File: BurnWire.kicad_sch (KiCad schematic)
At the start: 26 parts, among them J1 Conn_01x06_Pin, J2 282834-2, J3 Conn_01x02_Pin, J4 Conn_01x01_Pin, U1 ADP2303ARDZ

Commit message: Fix unrouted areas, board dimensions
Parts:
- C3, C4, C5: footprint Capacitor_SMD:C_0805_2012Metric_Pad1.18x1.45mm_HandSolder -> Capacitor_SMD:CP_Elec_5x5.4

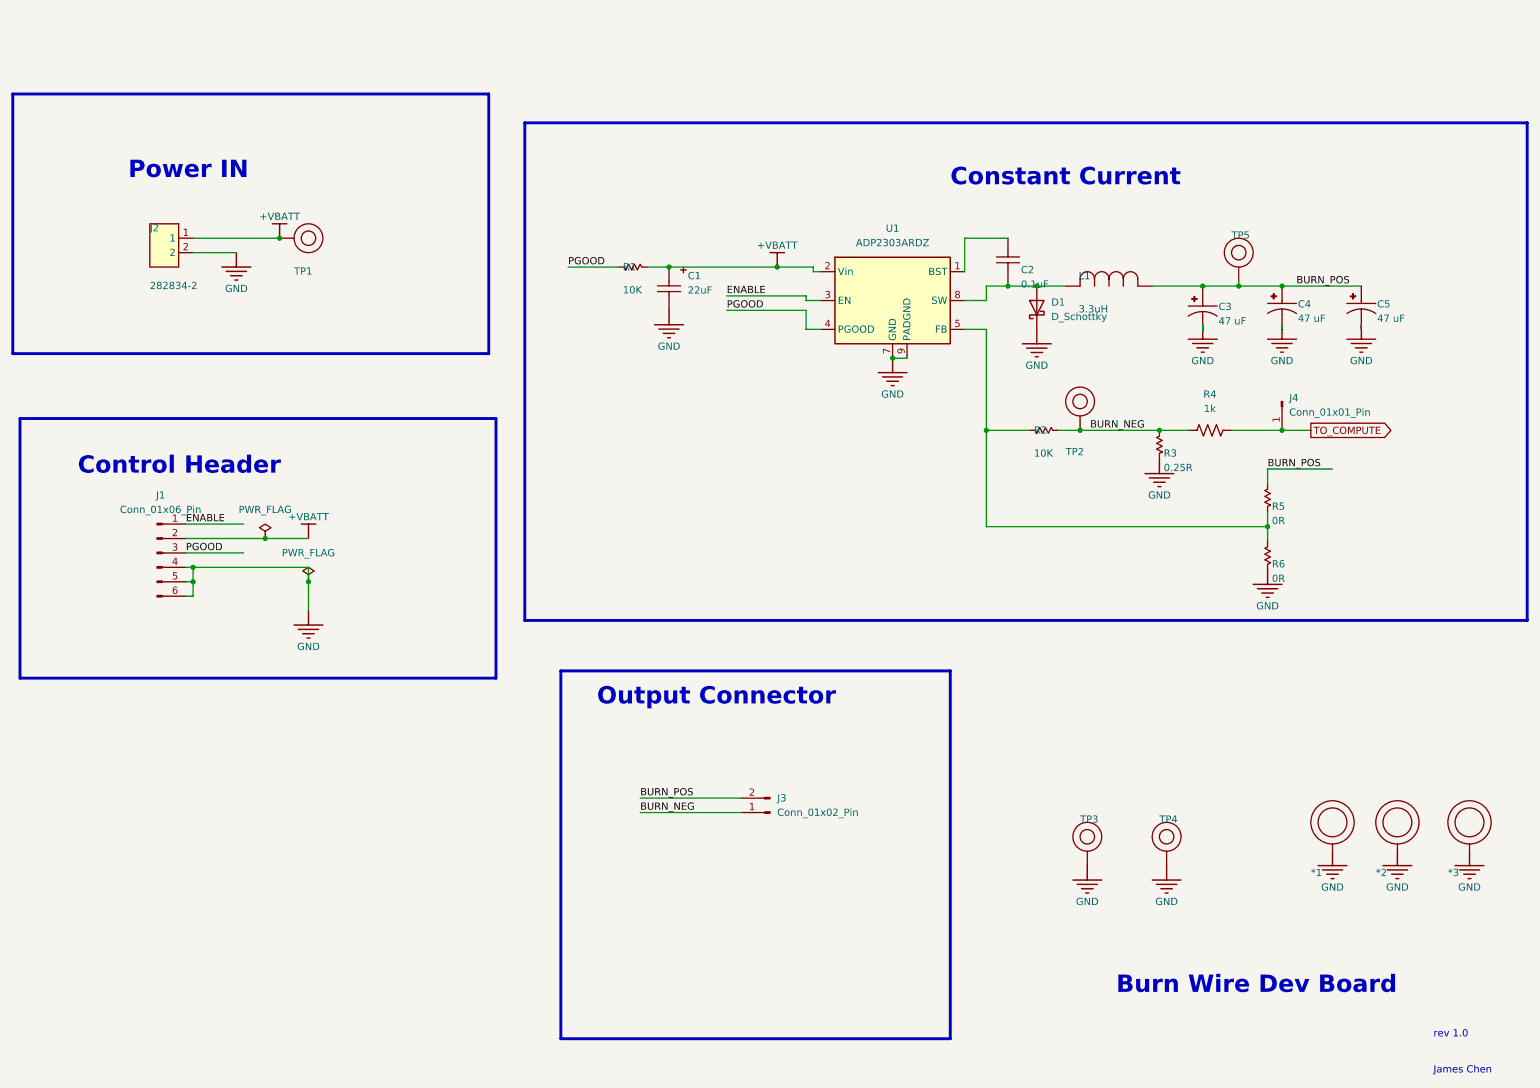
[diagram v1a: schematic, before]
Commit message: Removed all Altium references, fixed D1 direction, prepare for Rev 4.0
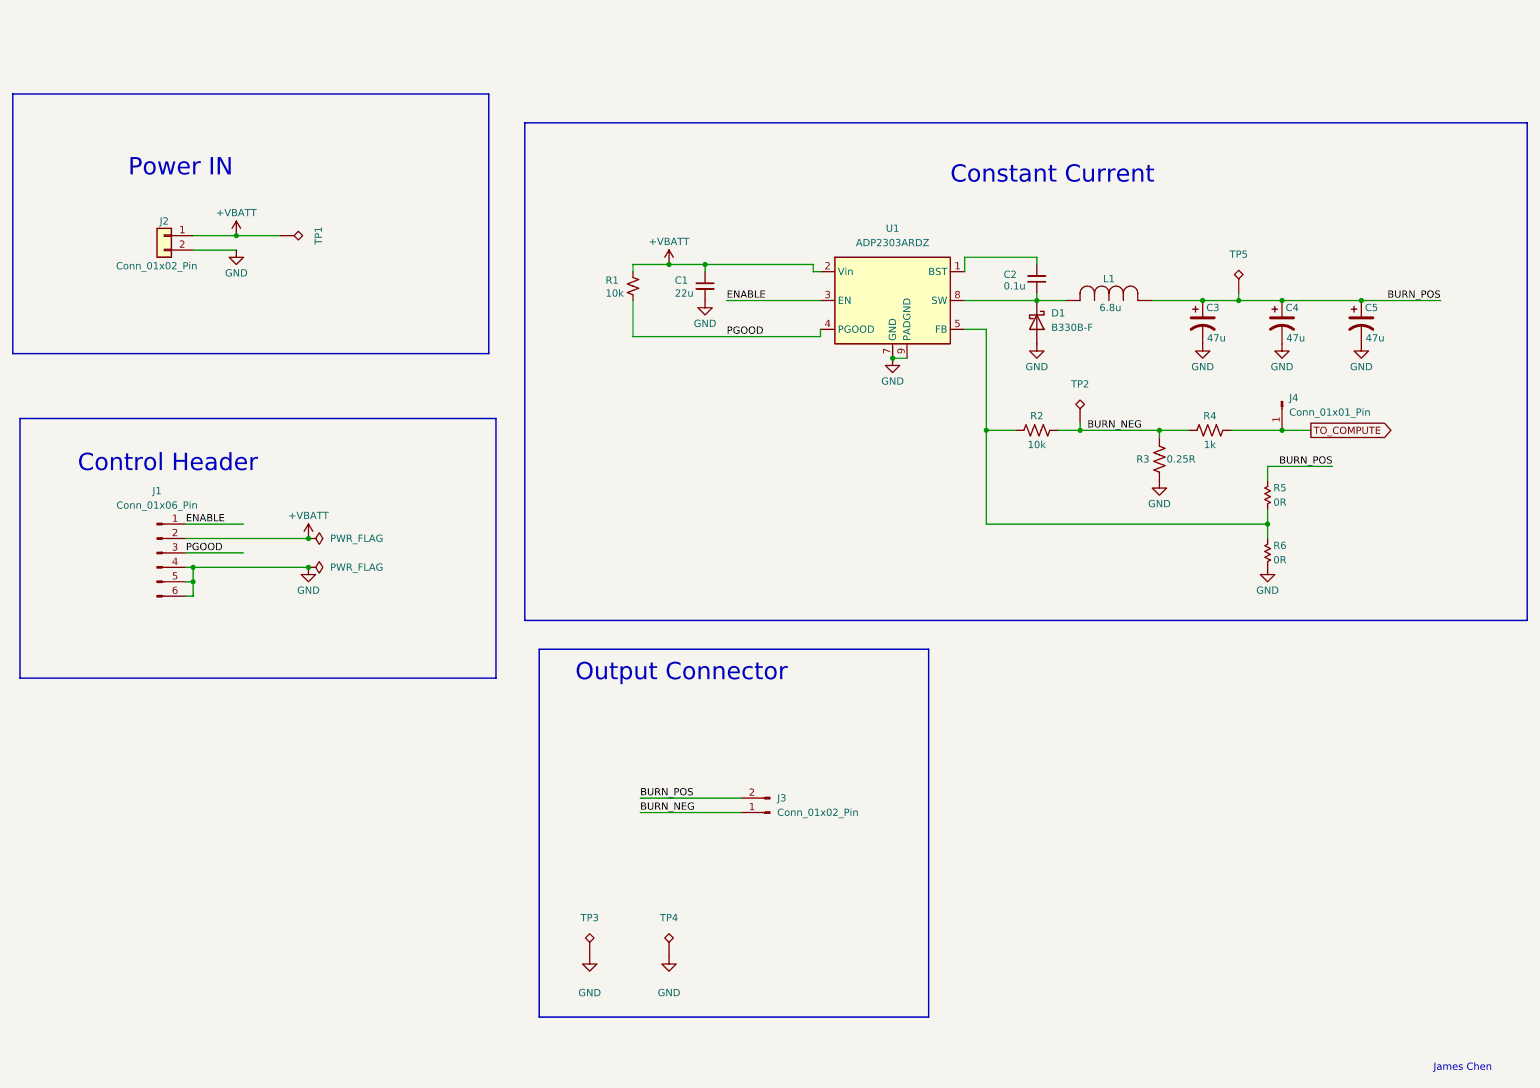
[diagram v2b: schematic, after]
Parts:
- removed *1, *2, *3: M2 Mounting, symbol RCU Board rev1.0:root_1_M2 Mounting_RCU Board rev1.0.SchLib
- C1: value 22uF -> 22u; symbol Burn Wire Dev Board:root_3_CT-225-M-20V-OTH-1206_Burn Wire Dev Board.SchLib -> Device:C_Small; ALTIUM_VALUE 22uF -> (none); COMPONENTLINK1DESCRIPTION Datasheet -> (none); COMPONENTLINK1URL * -> (none); COMPONENTLINK2DESCRIPTION Manufacturer Website -> (none); COMPONENTLINK2URL * -> (none); PART DESCRIPTION CAP TANT 22UF 10% 10V 1206 -> (none)
- C2: value 0.1uF -> 0.1u; symbol Burn Wire Dev Board:root_1_CC-104-K-25V-X7R-0603_Burn Wire Dev Board.SchLib -> Device:C_Small; ALTIUM_VALUE 0.1uF -> (none); COMPONENTLINK1DESCRIPTION Datasheet -> (none); COMPONENTLINK1URL https://ds.yuden.co.jp/TYCOMPAS/ut/detail?pn=TMK105BJ104KV-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 -> (none); COMPONENTLINK2DESCRIPTION Manufacturer Website -> (none); COMPONENTLINK2URL https://www.yuden.co.jp/or/ -> (none); PART DESCRIPTION 0.1 µF ±10% 25V Ceramic Capacitor X7R 0603 (1608 Metric) -> (none)
- C3, C4, C5: value 47 uF -> 47u; symbol Burn Wire Dev Board:root_3_CC-25SVPF47M_Burn Wire Dev Board.SchLib -> Device:C_Polarized_US; ALTIUM_VALUE 47 uF -> (none); COMPONENTLINK1DESCRIPTION Datasheet -> (none); COMPONENTLINK1URL * -> (none); COMPONENTLINK2DESCRIPTION Manufacture Website -> (none); COMPONENTLINK2URL * -> (none); PART DESCRIPTION CAP ALUM POLY 47UF 20% 25V SMD -> (none)
- D1: value D_Schottky -> B330B-F; footprint burn_wire:CR_SMB_320-345BE_DIO-L -> footprints:CR_SMB_320-345BE_DIO-L; DISTRIBUTOR (none) -> Digikey; DISTRIBUTOR PART # (none) -> B330B-FDICT-ND; MANUFACTURER (none) -> Diodes Incorporated; MANUFACTURER PART # (none) -> B330B-13-F
- J2: value 282834-2 -> Conn_01x02_Pin; symbol Burn Wire Dev Board:root_0_mirrored_J-282834-2_Burn Wire Dev Board.SchLib -> Connector_Generic:Conn_01x02
- L1: value 6.8 UH -> 6.8u; footprint burn_wire:IND_BOURNS_SRN6045 -> footprints:IND_BOURNS_SRN6045; symbol Burn Wire Dev Board:root_0_L-IHLP4040DZER6R8M01_Burn Wire Dev Board.SchLib -> imported_symbols:L-IHLP4040DZER6R8M01; ALTIUM_VALUE 3.3uH -> (none)
- R1: value 10K -> 10k; symbol Burn Wire Dev Board:root_0_RT-10K0-F-1/16W-0603_Burn Wire Dev Board.SchLib -> Device:R_Small_US; ALTIUM_VALUE 10K -> (none); COMPONENTLINK1DESCRIPTION Datasheet -> (none); COMPONENTLINK1URL https://www.vishay.com/docs/20035/dcrcwe3.pdf -> (none); COMPONENTLINK2DESCRIPTION Manufacturer Website -> (none); COMPONENTLINK2URL https://www.vishay.com/ -> (none); PART DESCRIPTION RES 10K OHM 1% 1/8W 0603 -> (none)
- R2: value 10K -> 10k; symbol Burn Wire Dev Board:root_0_RT-10K0-F-1/16W-0603_Burn Wire Dev Board.SchLib -> Device:R_US; ALTIUM_VALUE 10K -> (none); COMPONENTLINK1DESCRIPTION Datasheet -> (none); COMPONENTLINK1URL https://www.vishay.com/docs/20035/dcrcwe3.pdf -> (none); COMPONENTLINK2DESCRIPTION Manufacturer Website -> (none); COMPONENTLINK2URL https://www.vishay.com/ -> (none); PART DESCRIPTION RES 10K OHM 1% 1/8W 0603 -> (none)
- R3: symbol Burn Wire Dev Board:root_1_RT-0.25R0-F-3W-2010_Burn Wire Dev Board.SchLib -> Device:R_US; ALTIUM_VALUE 0.25R -> (none); COMPONENTLINK1DESCRIPTION Datasheet -> (none); COMPONENTLINK1URL https://www.vishay.com/docs/20035/dcrcwe3.pdf -> (none); COMPONENTLINK2DESCRIPTION Manufacturer Website -> (none); COMPONENTLINK2URL https://www.vishay.com/ -> (none); DISTRIBUTOR PART # 541-10112-1-ND -> 541-WSLT2010R2500FEA18CT-ND; MANUFACTURER PART # WSLT2010R5000FEA18 -> WSLT2010R2500FEA18; PART DESCRIPTION RES 0.5 OHM 1% 1W 2010 -> (none)
- R5, R6: symbol Burn Wire Dev Board:root_1_RT-0R00-F-1/10W-0603_Burn Wire Dev Board.SchLib -> imported_symbols:R_Small_US_Alt; ALTIUM_VALUE 0R -> (none); COMPONENTLINK1DESCRIPTION Datasheet -> (none); COMPONENTLINK1URL https://industrial.panasonic.com/ww/products/resistors/chip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 -> (none); COMPONENTLINK2DESCRIPTION Manufacturer Website -> (none); COMPONENTLINK2URL https://industrial.panasonic.com/ww/products/resistors/chip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 -> (none); PART DESCRIPTION 0 Ohms Jumper 0.1W, 1/10W Chip Resistor 0603 (1608 Metric) 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 -> (none)
- TP1: footprint Connector_PinSocket_2.54mm:PinSocket_1x01_P2.54mm_Vertical -> TestPoint:TestPoint_Loop_D1.80mm_Drill1.0mm_Beaded; symbol PowerManagmentBoard_V4.0:root_0_TP_PowerManagmentBoard_V4.0.SchLib -> Connector:TestPoint_Alt; COMPONENTLINK1DESCRIPTION Datasheet -> (none); COMPONENTLINK1URL https://industrial.panasonic.com/ww/products/resistors/chip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 -> (none); COMPONENTLINK2DESCRIPTION Manufacturer Website -> (none); COMPONENTLINK2URL https://industrial.panasonic.com/ww/products/resistors/chip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 -> (none)
- TP2, TP3, TP4, TP5: footprint Connector_PinSocket_2.54mm:PinSocket_1x01_P2.54mm_Vertical -> TestPoint:TestPoint_Loop_D1.80mm_Drill1.0mm_Beaded; symbol PowerManagmentBoard_V4.0:root_1_TP_PowerManagmentBoard_V4.0.SchLib -> Connector:TestPoint_Alt; COMPONENTLINK1DESCRIPTION Datasheet -> (none); COMPONENTLINK1URL https://industrial.panasonic.com/ww/products/resistors/chip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 -> (none); COMPONENTLINK2DESCRIPTION Manufacturer Website -> (none); COMPONENTLINK2URL https://industrial.panasonic.com/ww/products/resistors/chip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 -> (none)
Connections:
- net GND: now also D1.2 (A); no longer D1.1 (K)
- net at C2.1, L1.2, U1.8 (SW): now also D1.1 (K); no longer D1.2 (A)
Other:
- note removed: "Burn Wire Dev Board"
- note removed: "rev 1.0"
- moved on the sheet: D1, J2, L1, R1, R5, R6

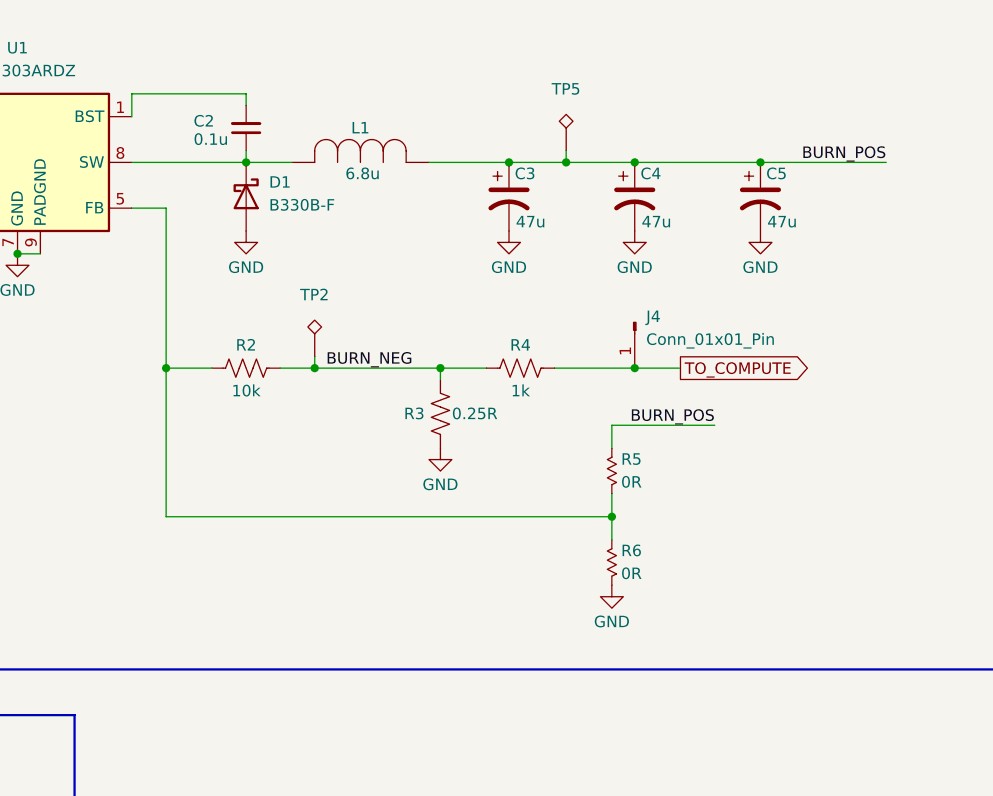
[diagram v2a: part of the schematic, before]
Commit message: change resistor to 0.5R and delete redundant resistors
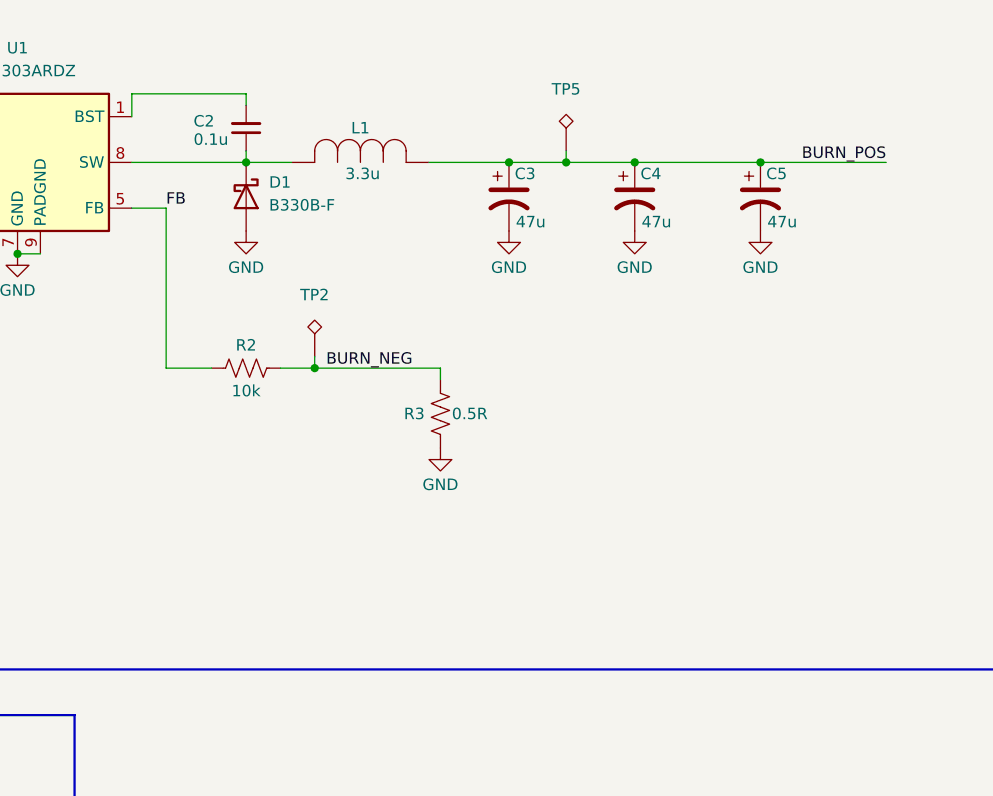
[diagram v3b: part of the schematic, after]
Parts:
- removed J4: Conn_01x01_Pin, Connector_PinSocket_2.54mm:PinSocket_1x01_P2.54mm_Horizontal, symbol Connector:Conn_01x01_Pin
- removed R4: 1k, Resistor_SMD:R_0805_2012Metric_Pad1.20x1.40mm_HandSolder, symbol Device:R_US
- removed R5, R6: 0R, Resistor_SMD:R_0603_1608Metric_Pad0.98x0.95mm_HandSolder, symbol imported_symbols:R_Small_US_Alt
- L1: value 6.8u -> 3.3u
- R3: value 0.25R -> 0.5R
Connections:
- net FB: now reaches R2.1, U1.5 (FB)

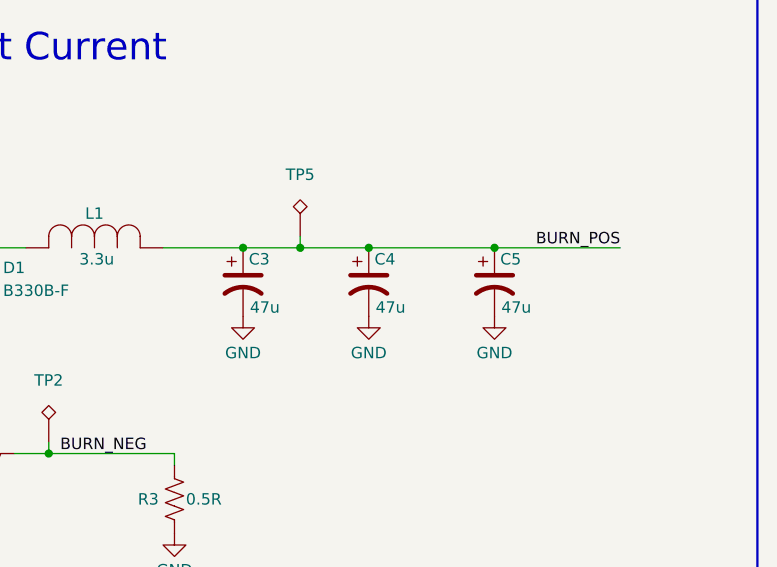
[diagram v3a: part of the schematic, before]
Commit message: switch to ceramic capacitors and fix via violations
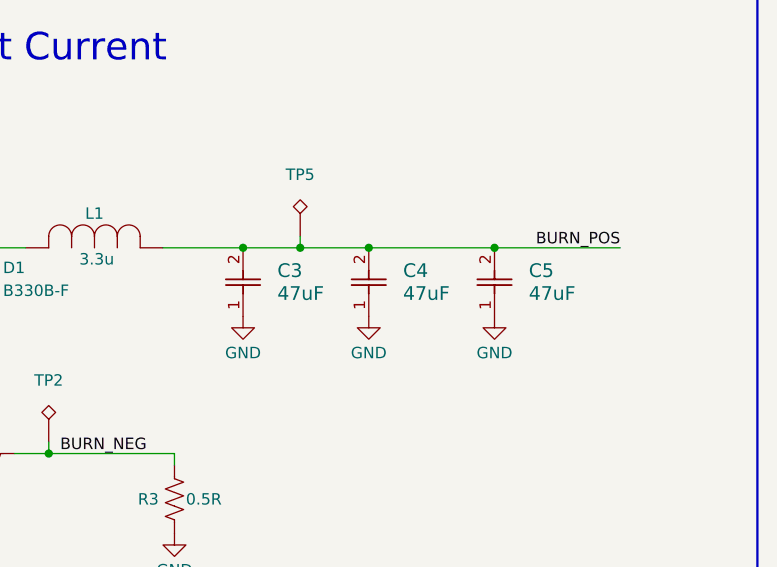
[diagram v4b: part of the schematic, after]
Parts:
- removed C3, C4, C5: 47u, Capacitor_SMD:CP_Elec_5x5.4, symbol Device:C_Polarized_US
- added C3, C4, C5: 47uF, footprints:CAP_GRM_32E_MUR, symbol GRM32ER60J476ME20L:GRM32ER60J476ME20L
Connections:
- net BURN_POS: now also C3.2, C4.2, C5.2
- net GND: now also C3.1, C4.1, C5.1
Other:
- title: (none) -> Burn Wire

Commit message: edit schematics
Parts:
- added J4: Conn_01x02_Pin, Connector_PinSocket_2.54mm:PinSocket_1x02_P2.54mm_Vertical, symbol Connector:Conn_01x02_Pin
- added Q1: DMC2053UVT, Package_TO_SOT_SMD:TSOT-23-6, symbol Transistor_FET:DMC2053UVT
- added R4, R5: 10k, Resistor_SMD:R_0805_2012Metric_Pad1.20x1.40mm_HandSolder, symbol Device:R_Small_US
- added R6: 1k, Resistor_SMD:R_0805_2012Metric_Pad1.20x1.40mm_HandSolder, symbol Device:R_US
- added TP6: TP, TestPoint:TestPoint_Loop_D1.80mm_Drill1.0mm_Beaded, symbol Connector:TestPoint_Alt
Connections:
- net +VBATT: now also Q1.2 (S)
- net BURN_NEG: now also R6.1
- net GND: now also J4.1 (Pin_1), Q1.5 (S), R4.1; no longer J1.5 (Pin_5), J1.6 (Pin_6)
- new net: Q1.3 (G), Q1.6 (D), R5.1
- new net BURN_POS_2: J4.2 (Pin_2), Q1.4 (D), R5.2, TP6.1
- new net ENABLE_BACKUP: J1.6 (Pin_6), Q1.1 (G), R4.2
- new net TO_COMPUTE: J1.5 (Pin_5), R6.2
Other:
- note added: "Constant Current with redundancy"
- note removed: "Constant Current"
- title: Burn Wire -> Burn Wire with Redundancy
- moved on the sheet: C1, C2, C3, C4, C5, D1, L1, R1, R2, R3, TP2, TP5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
